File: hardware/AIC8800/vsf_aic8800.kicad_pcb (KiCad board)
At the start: 2 copper layers, 31 parts, among them J0 USB_C_Receptacle_USB2.0, J1 Conn_01x20, J2 Conn_01x20, J3 Conn_02x05_Counter_Clockwise, Q0 AO3401, Q1 AO3402, SW0 SW_Push, SW1 SW_Push, U0 Module_AIC8800M

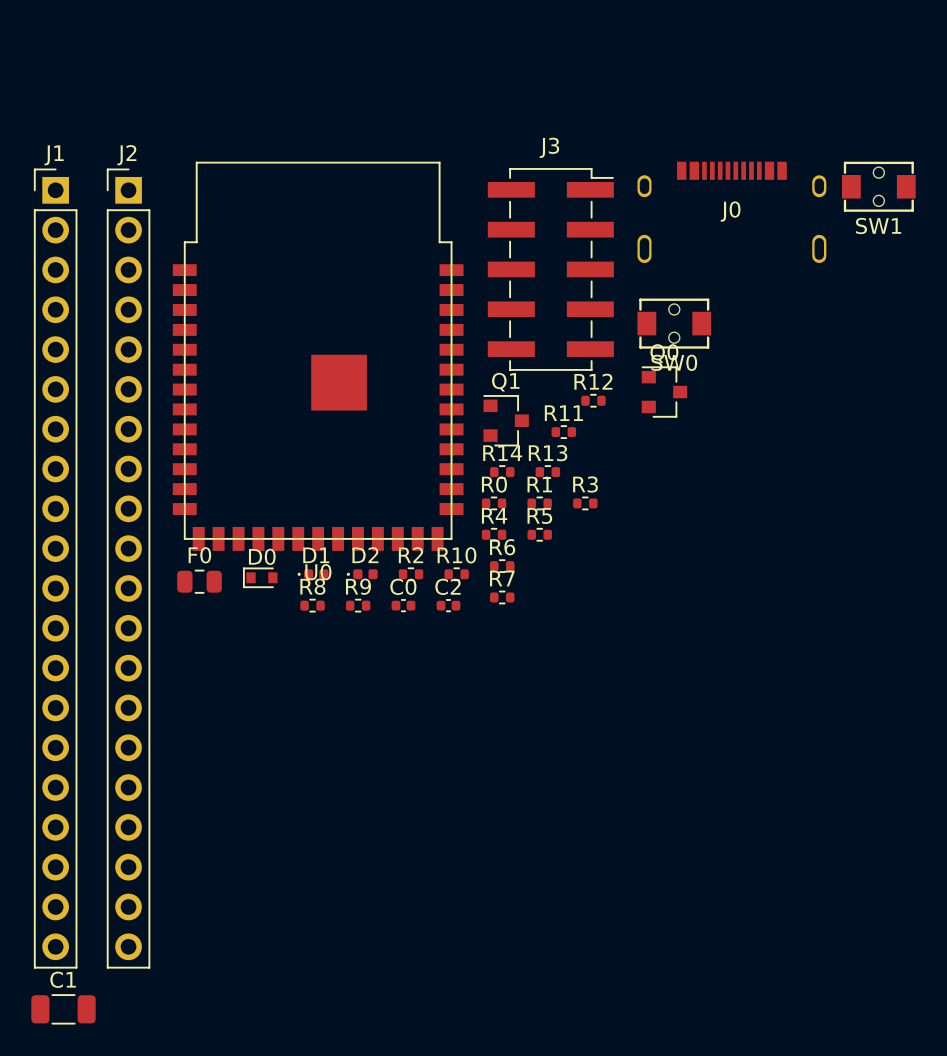
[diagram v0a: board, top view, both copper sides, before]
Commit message: [hardware/aic8800] update layout, prepare to route
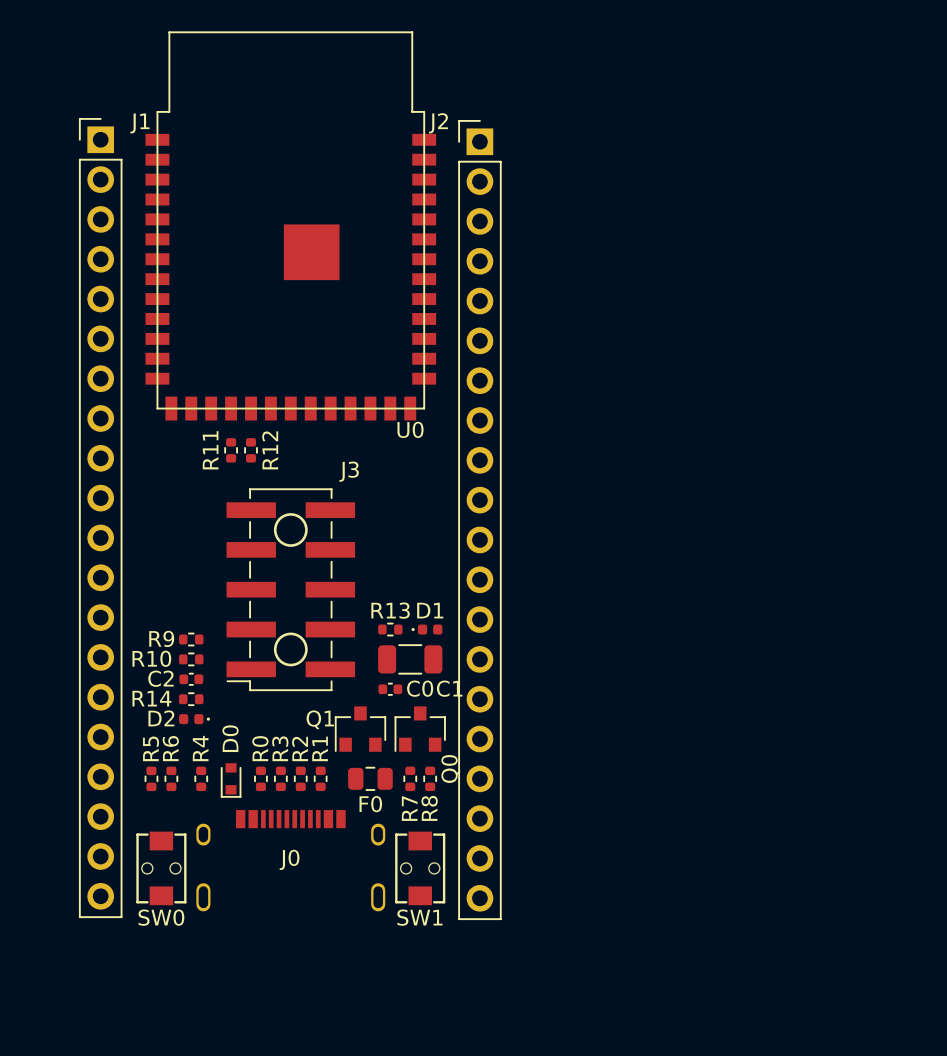
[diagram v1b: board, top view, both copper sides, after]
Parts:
- J3: footprint Connector_PinSocket_2.54mm:PinSocket_2x05_P2.54mm_Vertical_SMD -> simonqian:PinHeader_2x05_P2.54mm_Vertical_SMD_Clockwise
- moved SW1 52.4 mm to (225.4, 149.9), turned to 270 degrees
- moved J0 50.0 mm to (217.2, 149.2)
- moved SW0 47.7 mm to (208.9, 149.9), turned to 90 degrees
- moved C1 31.4 mm to (224.8, 136.5), turned to 180 degrees
- moved R5 29.3 mm to (208.3, 144.1), turned to 90 degrees
- moved Q0 26.6 mm to (225.4, 141.0), turned to 90 degrees
- moved J3 26.3 mm to (217.2, 132.1)
- moved R3 26.2 mm to (216.5, 144.1), turned to 270 degrees
- moved R6 25.1 mm to (209.6, 144.1), turned to 90 degrees
- moved R14 24.6 mm to (210.8, 139.1)
- moved R4 24.3 mm to (211.5, 144.1), turned to 270 degrees
- moved R0 23.0 mm to (215.3, 144.1), turned to 270 degrees
- moved J2 22.6 mm to (229.2, 103.5)
- moved R1 22.4 mm to (219.1, 144.1), turned to 270 degrees
- moved R12 22.1 mm to (214.6, 123.2), turned to 90 degrees
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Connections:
- J3 pad 4: /RST -> /PRST
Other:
- board text added: "A0"
- board text added: "A1"
- board text added: "A10"
- board text added: "A11"
- board text added: "A12"
- board text added: "A13"
- board text added: "A14"
- board text added: "A15"
- board text added: "A2"
- board text added: "A3"
- board text added: "A4"
- board text added: "A5"
- board text added: "A6"
- board text added: "A7"
- board text added: "A8"
- board text added: "A9"
- board text added: "B0"
- board text added: "B1"
- board text added: "B13"
- board text added: "B2"
- board text added: "B3"
- board text added: "B4"
- board text added: "B5"
- board text added: "B6"
- board text added: "B7"
- board text added: "DL"
- board text added: "GND"
- board text added: "PKEY"
- board text added: "PRST"
- board text added: "USB_5V"
- board text added: "USB_DM"
- board text added: "USB_DP"
- board text added: "V09"
- board text added: "V13"
- board text added: "V18"
- board text added: "V33"
- board text added: "VCC"
- board text added: "VSYS"

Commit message: [hardware/aic8800] update edge.cut
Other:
- board outline added: 27.9 x 52.1 mm

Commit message: [hardware/aic8800] minor tweak
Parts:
- moved J0 0.18 mm to (217.2, 149.0)
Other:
- outline, holes or cut-outs redrawn

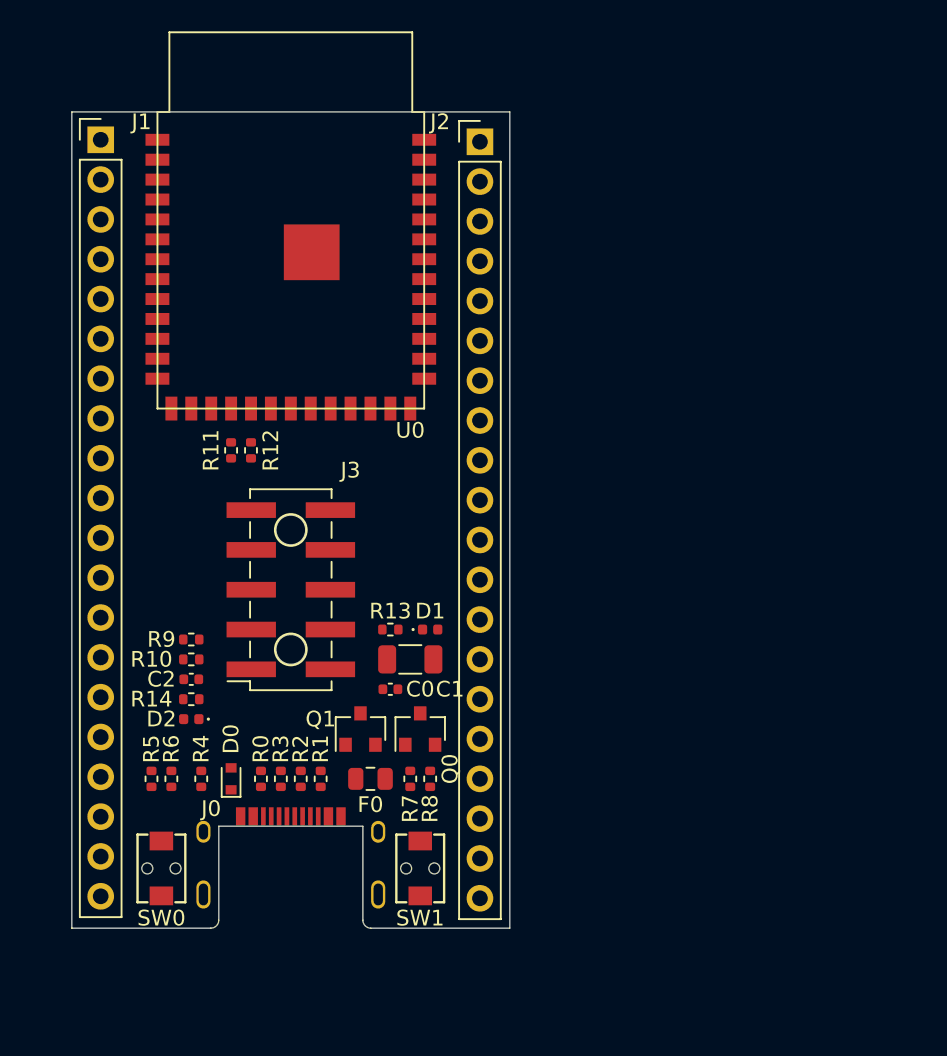
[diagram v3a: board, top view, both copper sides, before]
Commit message: [hardware/aic8800] update layout
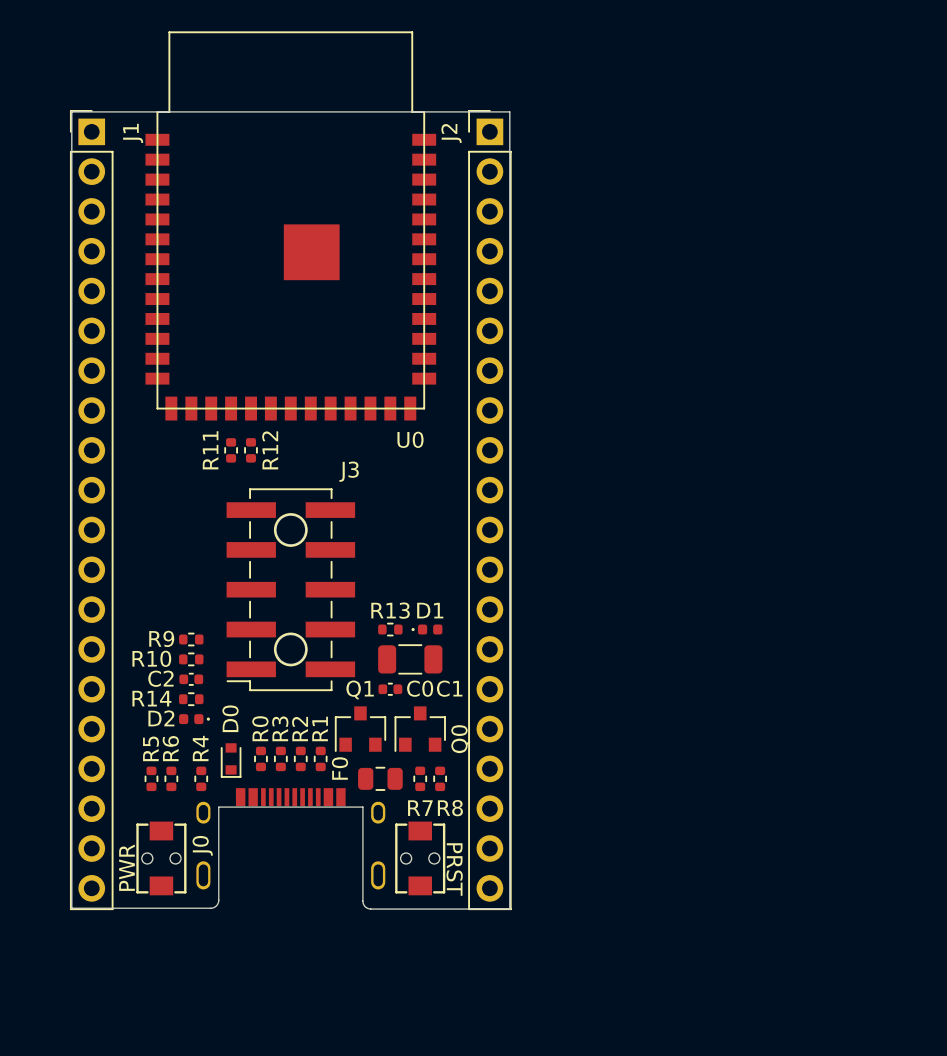
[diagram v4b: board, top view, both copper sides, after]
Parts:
- moved D0 1.27 mm to (213.4, 142.9)
- moved R0 1.27 mm to (215.3, 142.9)
- moved R1 1.27 mm to (219.1, 142.9)
- moved R2 1.27 mm to (217.8, 142.9)
- moved R3 1.27 mm to (216.5, 142.9)
- moved J0 1.22 mm to (217.2, 147.8)
- moved J2 0.90 mm to (229.9, 102.9)
- moved J1 0.76 mm to (204.5, 102.9)
- moved R7 0.64 mm to (225.4, 144.1)
- moved SW0 0.64 mm to (208.9, 149.2)
- moved SW1 0.64 mm to (225.4, 149.2)
- moved F0 0.63 mm to (222.9, 144.1)
- moved R8 0.63 mm to (226.7, 144.1)
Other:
- board size 27.9 x 52.1 mm -> 27.9 x 50.9 mm
- board text added: "PWR"

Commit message: [hardware/aic8800] route
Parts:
- R13, R14: value 4.7 -> 4.7K
- moved D1 18.9 mm to (208.5, 141.7), turned to 180 degrees
- moved R10 16.0 mm to (207.3, 120.9), turned to 180 degrees
- moved R9 15.8 mm to (207.3, 119.9), turned to 180 degrees
- moved R13 14.8 mm to (210.6, 141.7), turned to 180 degrees
- moved D2 2.29 mm to (208.5, 140.5)
- moved C0 1.91 mm to (225.4, 138.4)
- moved D0 1.53 mm to (212.3, 144.0), turned to 270 degrees
- moved C2 1.42 mm to (210.6, 139.2)
- moved R14 1.42 mm to (210.6, 140.5), turned to 180 degrees
- moved R7 1.27 mm to (226.7, 144.1), turned to 270 degrees
- moved R8 1.27 mm to (225.4, 144.1)
- moved R0 0.89 mm to (215.3, 142.0)
- moved R1 0.89 mm to (219.1, 142.0), turned to 90 degrees
- moved R2 0.89 mm to (217.8, 142.0)
- moved R3 0.89 mm to (216.5, 142.0)
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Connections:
- J1 pad 12: /VSYS -> /V18
- J1 pad 13: /V18 -> /V09
- J1 pad 20: /V09 -> /VSYS
- J2 pad 19: /PRST -> /DL
- J2 pad 20: /DL -> /PRST
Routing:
- net GND: track 0.00 -> 207.4 mm, vias 0 -> 13
- net /VSYS: track 0.00 -> 72.4 mm, vias 0 -> 2
- net /USB_5V: track 0.00 -> 60.1 mm, vias 0 -> 2
- net /PKEY: track 0.00 -> 50.4 mm, vias 0 -> 2
- net /USB_DM: track 0.00 -> 47.0 mm, vias 0 -> 2
- net /USB_DP: track 0.00 -> 46.2 mm, vias 0 -> 2
- net /VCC: track 0.00 -> 40.7 mm, vias 0 -> 1
- net /B7: track 0.00 -> 39.7 mm, vias 0 -> 1
- net /DL: track 0.00 -> 39.3 mm, vias 0 -> 2
- net /A0: track 0.00 -> 36.2 mm, vias 0 -> 2
- net /A1: track 0.00 -> 36.2 mm, vias 0 -> 2
- net /PRST: track 0.00 -> 34.8 mm, vias 0 -> 3
- net /B6: track 0.00 -> 30.2 mm
- net /A15: track 0.00 -> 30.0 mm
- net /A14: track 0.00 -> 26.7 mm
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- added copper zone on B.Cu, net GND
- added copper zone on F.Cu, net GND
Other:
- board size 27.9 x 50.9 mm -> 27.9 x 50.8 mm

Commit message: [hardware/aic8800] minor update
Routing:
- net GND: track 207.4 -> 212.9 mm, vias 13 -> 16
- net /DL: track 39.3 -> 42.4 mm
- net /VCC: track 40.7 -> 38.9 mm
- net /A8: track 21.4 -> 22.2 mm

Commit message: [hardware/aic8800] add 100uF cap on VCC
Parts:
- added C3: 100uF, Capacitor_SMD:C_1206_3216Metric, F.Cu at (207.5, 124.0)
- moved C2 12.6 mm to (207.5, 127.0)
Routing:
- net GND: track 212.9 -> 237.1 mm, vias 16 -> 20
- net /VCC: track 38.9 -> 40.2 mm
- net /V33: track 20.8 -> 21.9 mm
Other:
- net class Default: clearance 0.2 -> 0.1778; trace_width 0.25 -> 0.254; via_dia 0.8 -> 0.6096; via_drill 0.4 -> 0.3048
- rule trace_clearance: 0.2 -> 0.1778

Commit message: [hardware/aic8800] update
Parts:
- added R15: NC, Resistor_SMD:R_0402_1005Metric, F.Cu at (223.5, 132.1)
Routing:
- net GND: track 237.1 -> 239.9 mm
- net /DL: track 42.4 -> 43.4 mm
